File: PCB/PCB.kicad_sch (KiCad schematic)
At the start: 11 parts

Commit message: Footprint Design & Changes to Footprint/Schematics
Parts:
- D1, D2, D3, D4: footprint (none) -> LED_THT:LED_D3.0mm_Horizontal_O1.27mm_Z2.0mm_IRGrey
- R1, R2, R3, R4: footprint (none) -> Resistor_THT:R_Axial_DIN0918_L18.0mm_D9.0mm_P22.86mm_Horizontal
- U1: footprint (none) -> Arduino_Nano:Arduino_Nano
- U2: footprint (none) -> Timer_TM1637:TM1637
- U3: footprint (none) -> Sensor_HC-SR04:HC-SR04
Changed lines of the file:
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@@
 			)
 		)
-		(property "Footprint" ""
+		(property "Footprint" "LED_THT:LED_D3.0mm_Horizontal_O1.27mm_Z2.0mm_IRGrey"
 			(at 257.81 106.68 0)
 			(effects
@@
 			)
 		)
-		(property "Footprint" ""
+		(property "Footprint" "Resistor_THT:R_Axial_DIN0918_L18.0mm_D9.0mm_P22.86mm_Horizontal"
 			(at 207.772 91.44 90)
 			(effects
@@
 		(fields_autoplaced yes)
 		(property "Reference" "U3"
-			(at 198.12 99.6949 0)
+			(at 191.008 96.9009 0)
 			(effects
 				(font
@@
 		)
 		(property "Value" "~"
-			(at 198.12 101.6 0)
-			(effects
-				(font
-					(size 1.27 1.27)
-				)
-				(justify left)
-			)
-		)
-		(property "Footprint" ""
-			(at 179.07 95.25 0)
+			(at 191.008 98.806 0)
+			(effects
+				(font
+					(size 1.27 1.27)
+				)
+				(justify left)
+			)
+		)
+		(property "Footprint" "Sensor_HC-SR04:HC-SR04"
+			(at 179.324 86.106 0)
 			(effects
 				(font
@@
 			)
 		)
-		(property "Footprint" ""
+		(property "Footprint" "Arduino_Nano:Arduino_Nano"
 			(at 55.88 110.49 0)
 			(effects
@@
 			)
 		)
-		(property "Footprint" ""
+		(property "Footprint" "Resistor_THT:R_Axial_DIN0918_L18.0mm_D9.0mm_P22.86mm_Horizontal"
 			(at 230.632 91.44 90)
 			(effects
@@
 		(fields_autoplaced yes)
 		(property "Reference" "U2"
-			(at 147.32 97.1549 0)
+			(at 141.478 93.8529 0)
 			(effects
 				(font
@@
 		)
 		(property "Value" "~"
-			(at 147.32 99.06 0)
-			(effects
-				(font
-					(size 1.27 1.27)
-				)
-				(justify left)
-			)
-		)
-		(property "Footprint" ""
+			(at 141.478 95.758 0)
+			(effects
+				(font
+					(size 1.27 1.27)
+				)
+				(justify left)
+			)
+		)
+		(property "Footprint" "Timer_TM1637:TM1637"
 			(at 125.73 101.6 0)
 			(effects
@@
 			)
 		)
-		(property "Footprint" ""
+		(property "Footprint" "Resistor_THT:R_Axial_DIN0918_L18.0mm_D9.0mm_P22.86mm_Horizontal"
 			(at 256.032 91.44 90)
 			(effects
@@
 			)
 		)
-		(property "Footprint" ""
+		(property "Footprint" "LED_THT:LED_D3.0mm_Horizontal_O1.27mm_Z2.0mm_IRGrey"
 			(at 220.98 106.68 0)
 			(effects
@@
 			)
 		)
-		(property "Footprint" ""
+		(property "Footprint" "Resistor_THT:R_Axial_DIN0918_L18.0mm_D9.0mm_P22.86mm_Horizontal"
 			(at 219.202 91.44 90)
 			(effects
@@
 			)
 		)
-		(property "Footprint" ""
+		(property "Footprint" "LED_THT:LED_D3.0mm_Horizontal_O1.27mm_Z2.0mm_IRGrey"
 			(at 209.55 106.68 0)
 			(effects
@@
 			)
 		)
-		(property "Footprint" ""
+		(property "Footprint" "LED_THT:LED_D3.0mm_Horizontal_O1.27mm_Z2.0mm_IRGrey"
 			(at 232.41 106.68 0)
 			(effects

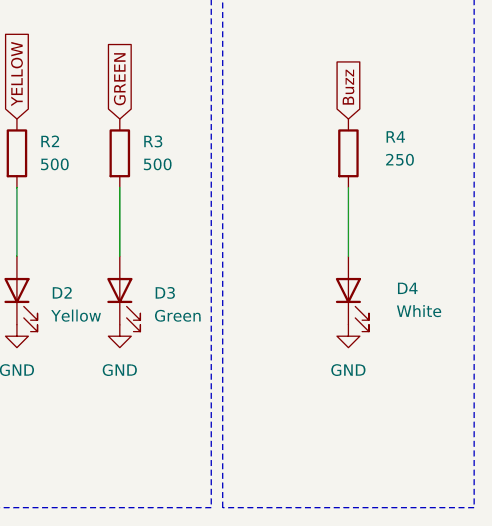
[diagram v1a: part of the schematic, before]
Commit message: Arrangment of component footprints on PCB
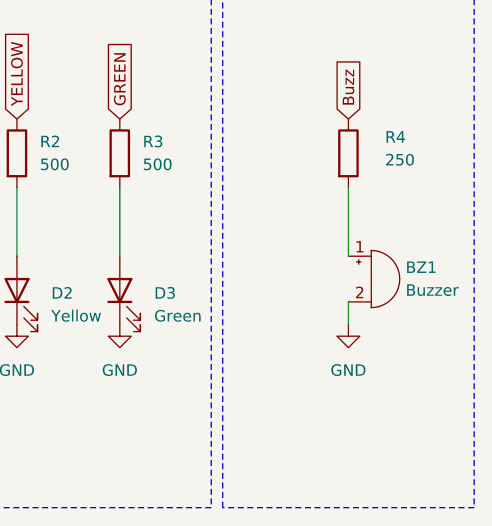
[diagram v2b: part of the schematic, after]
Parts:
- removed D4: White, LED_THT:LED_D3.0mm_Horizontal_O1.27mm_Z2.0mm_IRGrey, symbol Device:LED
- added BZ1: Buzzer, Buzzer_Beeper:Buzzer_12x9.5RM7.6, symbol Device:Buzzer
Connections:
- net GND: now also BZ1.2 (-)
- net at R4.2: now also BZ1.1 (+)
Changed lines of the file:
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@@
+	(wire
+		(pts
+			(xy 257.81 107.95) (xy 257.81 110.49)
+		)
+		(stroke
+			(width 0)
+			(type default)
+		)
+	)
 	(wire
 		(pts
@@
 	)
 	(symbol
-		(lib_id "Device:LED")
-		(at 257.81 106.68 90)
-		(unit 1)
-		(exclude_from_sim no)
-		(in_bom yes)
-		(on_board yes)
-		(dnp no)
-		(property "Reference" "D4"
-			(at 263.144 106.4895 90)
-			(effects
-				(font
-					(size 1.27 1.27)
-				)
-				(justify right)
-			)
-		)
-		(property "Value" "White"
-			(at 263.144 109.0295 90)
-			(effects
-				(font
-					(size 1.27 1.27)
-				)
-				(justify right)
-			)
-		)
-		(property "Footprint" "LED_THT:LED_D3.0mm_Horizontal_O1.27mm_Z2.0mm_IRGrey"
-			(at 257.81 106.68 0)
-			(effects
-				(font
-					(size 1.27 1.27)
-				)
-				(hide yes)
-			)
-		)
-		(property "Datasheet" "~"
-			(at 257.81 106.68 0)
-			(effects
-				(font
-					(size 1.27 1.27)
-				)
-				(hide yes)
-			)
-		)
-		(property "Description" "Light emitting diode"
-			(at 257.81 106.68 0)
-			(effects
-				(font
-					(size 1.27 1.27)
-				)
-				(hide yes)
-			)
-		)
-		(pin "2"
-		)
-		(pin "1"
-		)
-		(instances
-			(project ""
-				(path "/a42eb789-c298-48ff-a9e1-bce89900549c"
-					(reference "D4")
-					(unit 1)
-				)
-			)
-		)
-	)
-	(symbol
 		(lib_id "Device:R")
 		(at 209.55 91.44 0)
@@
 					(unit 1)
 				)
+			)
+		)
+	)
+	(symbol
+		(lib_id "Device:Buzzer")
+		(at 260.35 105.41 0)
+		(unit 1)
+		(exclude_from_sim no)
+		(in_bom yes)
+		(on_board yes)
+		(dnp no)
+		(fields_autoplaced yes)
+		(property "Reference" "BZ1"
+			(at 264.16 104.1399 0)
+			(effects
+				(font
+					(size 1.27 1.27)
+				)
+				(justify left)
+			)
+		)
+		(property "Value" "Buzzer"
+			(at 264.16 106.6799 0)
+			(effects
+				(font
+					(size 1.27 1.27)
+				)
+				(justify left)
+			)
+		)
+		(property "Footprint" "Buzzer_Beeper:Buzzer_12x9.5RM7.6"
+			(at 259.715 102.87 90)
+			(effects
+				(font
+					(size 1.27 1.27)
+				)
+				(hide yes)
+			)
+		)
+		(property "Datasheet" "~"
+			(at 259.715 102.87 90)
+			(effects
+				(font
+					(size 1.27 1.27)
+				)
+				(hide yes)
+			)
+		)
+		(property "Description" "Buzzer, polarized"
+			(at 260.35 105.41 0)
+			(effects
+				(font
+					(size 1.27 1.27)
+				)
+				(hide yes)
+			)
+		)
+		(pin "1"
+		)
+		(pin "2"
+		)
+		(instances
+			(project ""
+				(path "/a42eb789-c298-48ff-a9e1-bce89900549c"
+					(reference "BZ1")
+					(unit 1)
+				)

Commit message: Routing & DRC of PCB
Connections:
- net Source renamed Power

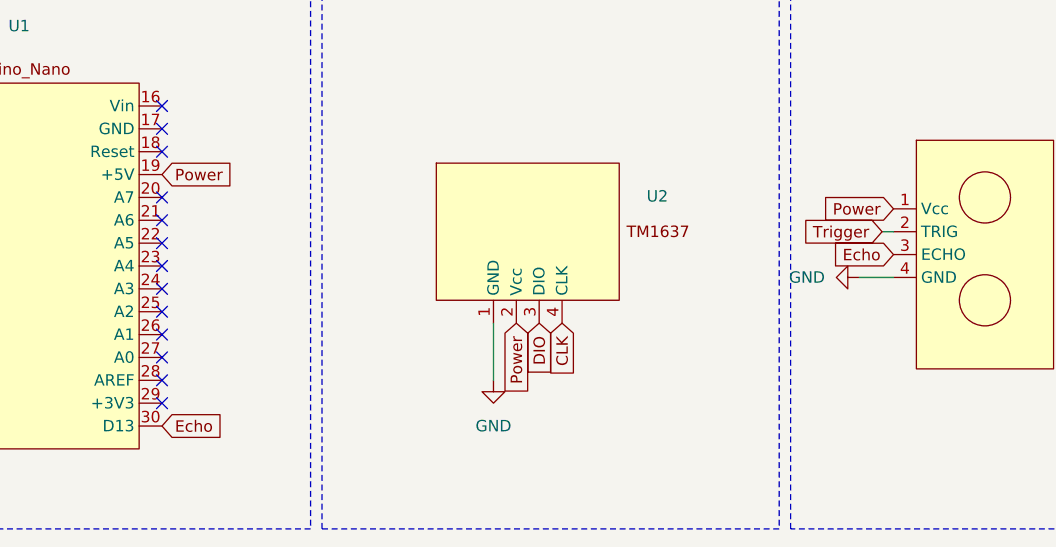
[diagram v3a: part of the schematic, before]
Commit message: Small changes to schematic (for DRC warnings)
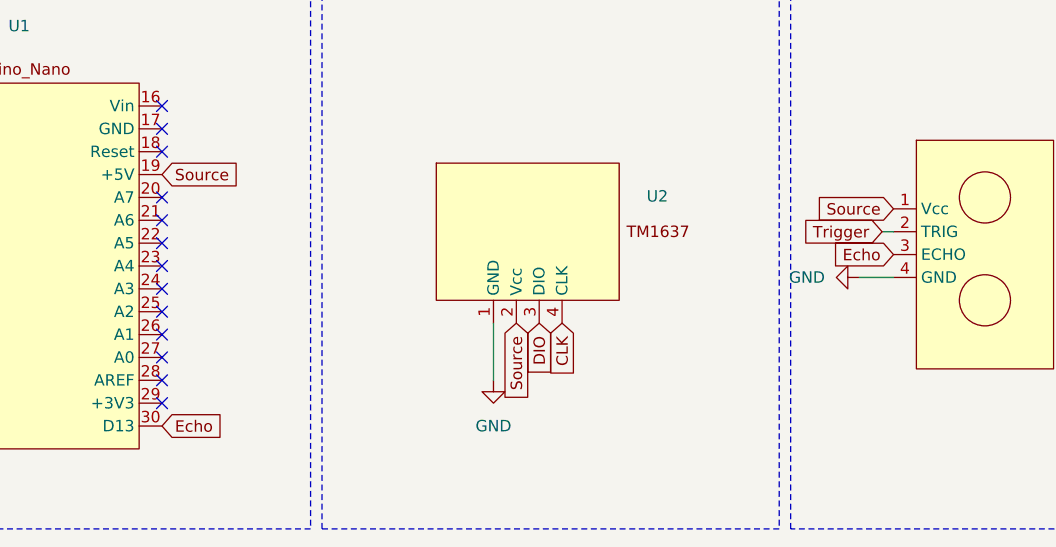
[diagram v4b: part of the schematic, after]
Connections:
- net Power renamed Source
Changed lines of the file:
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@@
 		)
 	)
-	(global_label "Power"
+	(global_label "Source"
 		(shape input)
 		(at 127 107.95 270)
@@
 		)
 		(property "Intersheetrefs" "${INTERSHEET_REFS}"
-			(at 127 116.5595 90)
+			(at 127 117.4061 90)
 			(effects
 				(font
@@
 		)
 	)
-	(global_label "Power"
+	(global_label "Source"
 		(shape input)
 		(at 168.91 95.25 180)
@@
 		)
 		(property "Intersheetrefs" "${INTERSHEET_REFS}"
-			(at 160.3005 95.25 0)
+			(at 159.4539 95.25 0)
 			(effects
 				(font
@@
 		)
 	)
-	(global_label "Power"
+	(global_label "Source"
 		(shape input)
 		(at 87.63 91.44 0)
@@
 		)
 		(property "Intersheetrefs" "${INTERSHEET_REFS}"
-			(at 96.2395 91.44 0)
+			(at 97.0861 91.44 0)
 			(effects
 				(font
